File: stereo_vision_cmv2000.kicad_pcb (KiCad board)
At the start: 4 copper layers, 50 x 40 mm, 79 parts, among them P101 CONN_51, P102 CONN_33, U201 AP1084, U202 MCP1826S, U203 RT9017-20GBR, U301 CMV2000, U401 MOUNTHOLE, U402 MOUNTHOLE, U403 MOUNTHOLE, U404 MOUNTHOLE, U405 MOUNTHOLE, U406 MOUNTHOLE, U407 MOUNTHOLE, U408 MOUNTHOLE, U501 24AA025E48

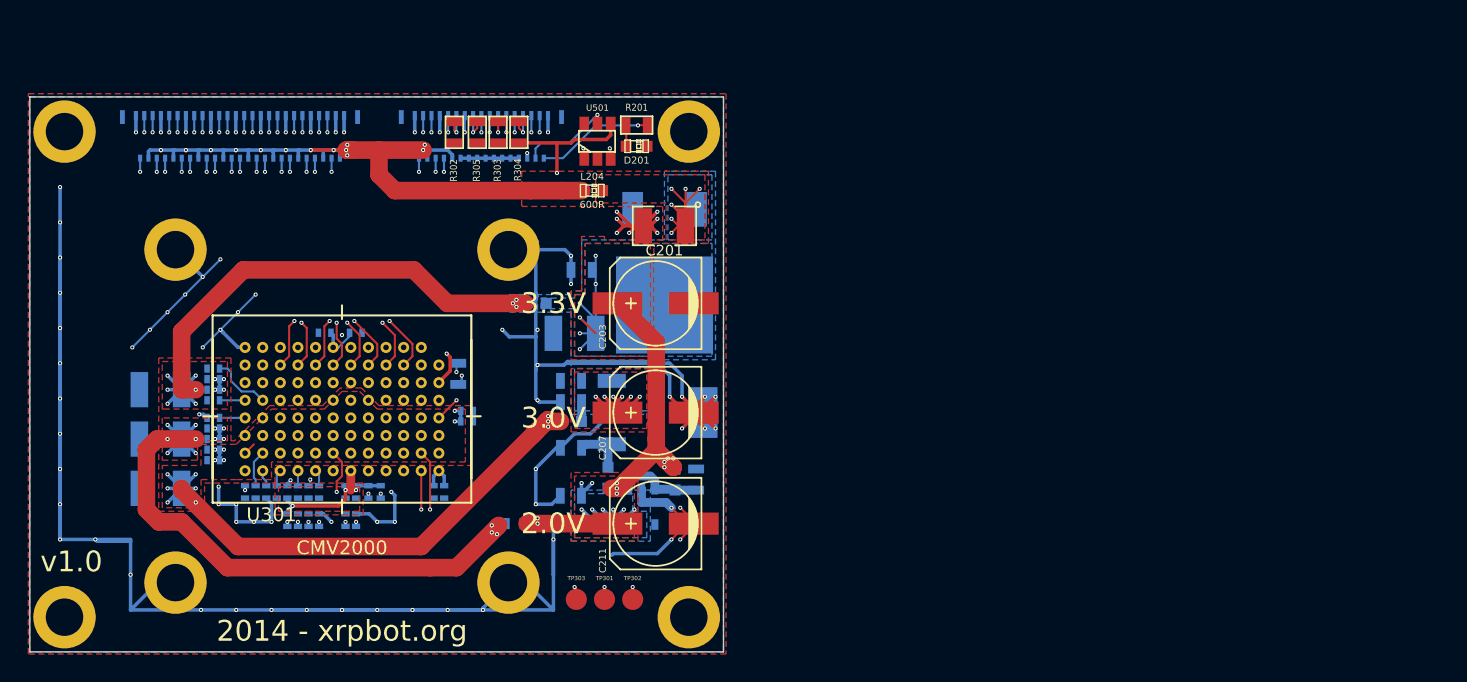
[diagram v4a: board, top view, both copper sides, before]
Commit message: Increase via size
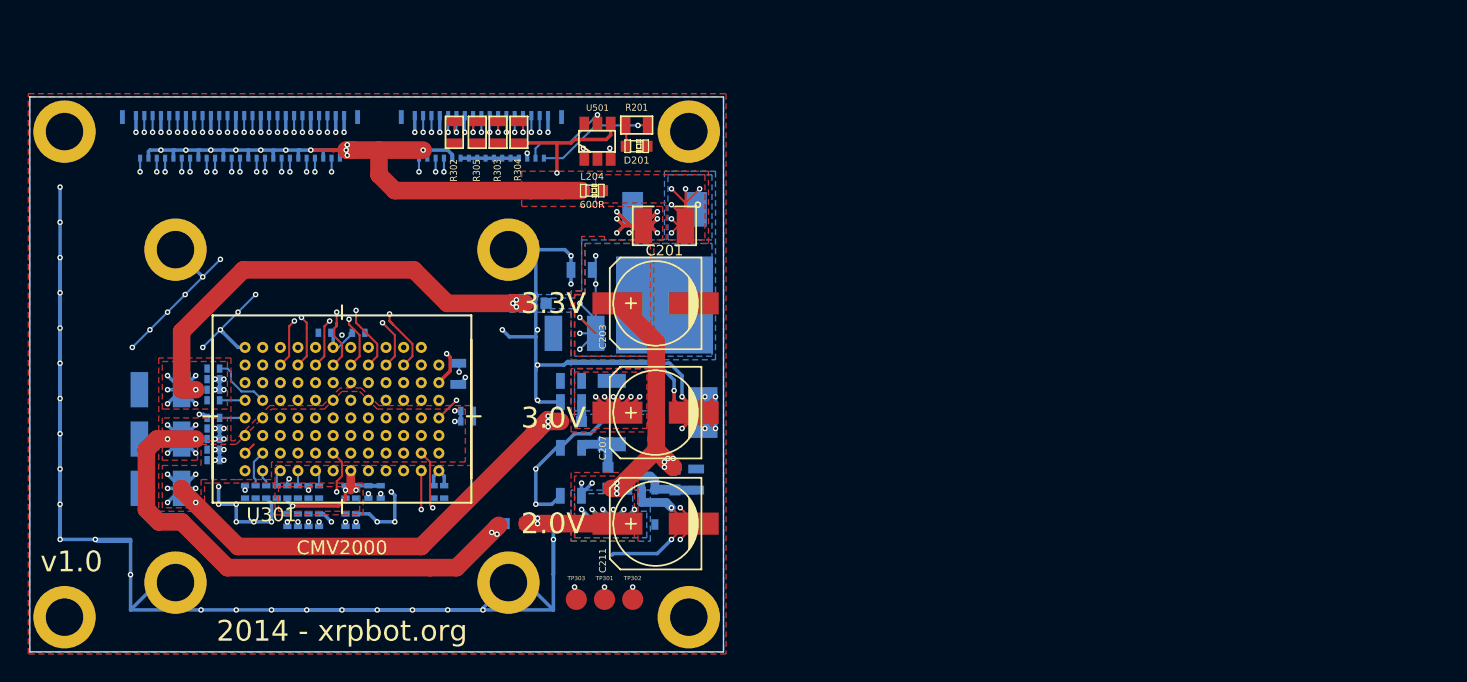
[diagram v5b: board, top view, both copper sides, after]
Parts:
- moved C306 0.20 mm to (132.0, 110.1)
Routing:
- net /Sheet53D8E0E2/SDA: track 8.12 -> 9.09 mm
- net /CMV2000/3.3V: track 107.3 -> 108.2 mm
- net /CMV2000/LVDS_CLK_IN_P: track 24.4 -> 25.2 mm
- net Net-(C340-Pad2): track 4.04 -> 4.81 mm
- net /CMV2000/LVDS_10_N: track 21.8 -> 22.4 mm
- net /CMV2000/SYS_RES_N: track 40.8 -> 40.2 mm
- net GND: track 304.0 -> 304.5 mm
- net /CMV2000/2.0V: track 66.2 -> 65.9 mm, vias 13 -> 12
- net /Power Supply/5V: vias 13 -> 11
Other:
- net class Default: via_dia 0.3 -> 0.4; via_drill 0.25 -> 0.3
- net class Power: via_dia 0.3 -> 0.4; via_drill 0.25 -> 0.3
- net class Power_thick: via_dia 0.3 -> 0.4; via_drill 0.25 -> 0.3
- net class power_thin: via_dia 0.3 -> 0.4; via_drill 0.25 -> 0.3
- rule via_min_size: 0.3 -> 0.4

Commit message: rework connector design and differential routing
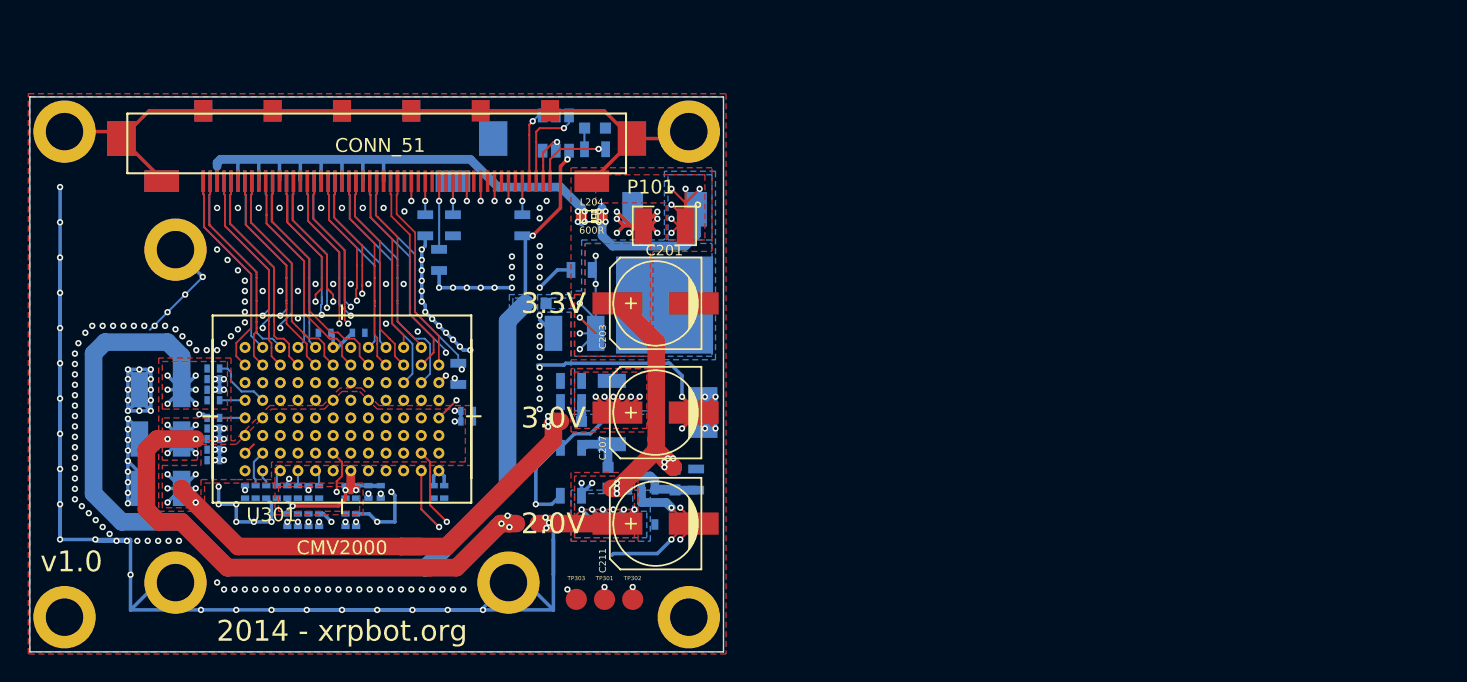
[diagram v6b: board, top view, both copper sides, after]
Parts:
- removed U406: MOUNTHOLE, owncomp:MOUNTING_HOLE
- D201, R201, R302, R303, R304, R305, U501: moved to B.Cu
- P101: footprint owncomp:MOLEX_FPC_0.3mm_51pin -> owncomp:FI-RE51S-HF-R1500; moved to F.Cu
- P102: value CONN_33 -> CONN_31; footprint owncomp:MOLEX_FPC_0.3mm_33pin -> owncomp:FI-RE31S-HF-R1500
- moved P102 13.2 mm to (128.3, 98.6)
- moved P101 10.7 mm to (133.3, 98.6), turned to 180 degrees
- moved R305 9.60 mm to (137.8, 104.8)
- moved R303 7.45 mm to (138.8, 102.3)
- moved R302 7.02 mm to (136.8, 102.3)
- moved R304 6.70 mm to (143.8, 102.3)
- moved R201 3.47 mm to (149.0, 96.8)
- moved D201 3.27 mm to (149.0, 95.3)
- moved U501 3.06 mm to (146.2, 95.7)
- moved L204 1.85 mm to (148.8, 101.7)
- moved L201 1.02 mm to (144.3, 123.8)
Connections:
- P101 pad 1: GND -> /Power Supply/LED_3.3V
- P101 pad 10: /Power Supply/5V -> GND
- P101 pad 11: /CMV2000/LVDS_13_N -> /CMV2000/SPI_OUT
- P101 pad 12: /CMV2000/LVDS_13_P -> GND
- P101 pad 13: GND -> /CMV2000/SPI_IN
- P101 pad 14: /CMV2000/LVDS_14_N -> GND
- P101 pad 15: /CMV2000/LVDS_14_P -> /CMV2000/T_EXP1
- P101 pad 16: /Power Supply/5V -> GND
- P101 pad 17: /CMV2000/LVDS_12_N -> /CMV2000/T_EXP2
- P101 pad 18: /CMV2000/LVDS_12_P -> GND
- P101 pad 19: GND -> /CMV2000/FRAME_REQ
- P101 pad 2: /CMV2000/LVDS_CLK_OUT_N -> /Sheet53D8E0E2/A0
- P101 pad 20: /CMV2000/LVDS_11_N -> GND
- P101 pad 21: /CMV2000/LVDS_11_P -> /CMV2000/CLK_IN
- P101 pad 22: /Power Supply/5V -> GND
- P101 pad 23: /CMV2000/LVDS_10_N -> /CMV2000/LVDS_CTR_N
- P101 pad 24: /CMV2000/LVDS_10_P -> /CMV2000/LVDS_CTR_P
- P101 pad 26: /CMV2000/LVDS_9_N -> /CMV2000/LVDS_2_N
- P101 pad 27: /CMV2000/LVDS_9_P -> /CMV2000/LVDS_2_P
- P101 pad 28: /Power Supply/5V -> GND
- P101 pad 29: /CMV2000/LVDS_7_N -> /CMV2000/LVDS_4_N
- P101 pad 3: /CMV2000/LVDS_CLK_OUT_P -> /Sheet53D8E0E2/SDA
- P101 pad 30: /CMV2000/LVDS_7_P -> /CMV2000/LVDS_4_P
- P101 pad 32: /CMV2000/LVDS_8_N -> /CMV2000/LVDS_3_N
- P101 pad 33: /CMV2000/LVDS_8_P -> /CMV2000/LVDS_3_P
- P101 pad 34: /Power Supply/5V -> GND
- P101 pad 35: /CMV2000/LVDS_5_N -> /CMV2000/LVDS_8_N
- P101 pad 36: /CMV2000/LVDS_5_P -> /CMV2000/LVDS_8_P
- P101 pad 38: /CMV2000/LVDS_6_N -> /CMV2000/LVDS_9_N
- P101 pad 39: /CMV2000/LVDS_6_P -> /CMV2000/LVDS_9_P
- P101 pad 4: /Power Supply/5V -> /Sheet53D8E0E2/SCL
- P101 pad 40: /Power Supply/5V -> GND
- P101 pad 41: /CMV2000/LVDS_4_N -> /CMV2000/LVDS_7_N
- P101 pad 42: /CMV2000/LVDS_4_P -> /CMV2000/LVDS_7_P
- P101 pad 44: /CMV2000/LVDS_3_N -> /CMV2000/LVDS_10_N
- P101 pad 45: /CMV2000/LVDS_3_P -> /CMV2000/LVDS_10_P
- P101 pad 46: /Power Supply/5V -> GND
- P101 pad 47: /CMV2000/LVDS_2_N -> /CMV2000/LVDS_13_N
- P101 pad 48: /CMV2000/LVDS_2_P -> /CMV2000/LVDS_13_P
- P101 pad 5: /CMV2000/LVDS_15_N -> /CMV2000/SYS_RES_N
- P101 pad 50: /Power Supply/5V -> /CMV2000/LVDS_CLK_OUT_N
- P101 pad 51: GND -> /CMV2000/LVDS_CLK_OUT_P
- P101 pad 52: (no net) -> GND
- P101 pad 53: (no net) -> GND
- P101 pad 6: /CMV2000/LVDS_15_P -> GND
- P101 pad 7: GND -> /CMV2000/SPI_CLK
- P101 pad 8: /CMV2000/LVDS_16_N -> GND
- P101 pad 9: /CMV2000/LVDS_16_P -> /CMV2000/SPI_EN
- P102 pad 1: GND -> /CMV2000/LVDS_15_P
- P102 pad 10: /Power Supply/5V -> /CMV2000/LVDS_12_P
- P102 pad 11: /CMV2000/FRAME_REQ -> /CMV2000/LVDS_12_N
- P102 pad 12: GND -> /Power Supply/5V
- P102 pad 13: /CMV2000/CLK_IN -> /CMV2000/LVDS_11_P
- P102 pad 14: GND -> /CMV2000/LVDS_11_N
- P102 pad 15: /CMV2000/T_EXP2 -> /Power Supply/5V
- P102 pad 16: GND -> /CMV2000/LVDS_6_P
- P102 pad 17: /CMV2000/SPI_IN -> /CMV2000/LVDS_6_N
- P102 pad 18: GND -> /Power Supply/5V
- P102 pad 19: /CMV2000/SPI_OUT -> /CMV2000/LVDS_5_P
- P102 pad 2: /CMV2000/LVDS_1_N -> /CMV2000/LVDS_15_N
- P102 pad 20: GND -> /CMV2000/LVDS_5_N
- P102 pad 21: /CMV2000/T_EXP1 -> /Power Supply/5V
- P102 pad 22: GND -> /CMV2000/LVDS_1_P
- P102 pad 23: /CMV2000/SPI_CLK -> /CMV2000/LVDS_1_N
- P102 pad 24: GND -> /Power Supply/5V
- P102 pad 25: /CMV2000/SPI_EN -> /CMV2000/LVDS_CLK_IN_P
- P102 pad 26: GND -> /CMV2000/LVDS_CLK_IN_N
- P102 pad 27: /CMV2000/SYS_RES_N -> /Power Supply/5V
- P102 pad 28: /Sheet53D8E0E2/SCL -> Net-(P102-Pad28)
- P102 pad 29: /Sheet53D8E0E2/SDA -> Net-(P102-Pad29)
- P102 pad 3: /CMV2000/LVDS_1_P -> /Power Supply/5V
- P102 pad 30: /Sheet53D8E0E2/A0 -> Net-(P102-Pad30)
- P102 pad 32: /Power Supply/LED_3.3V -> GND
- P102 pad 4: /Power Supply/5V -> /CMV2000/LVDS_16_P
- P102 pad 5: /CMV2000/LVDS_CTR_N -> /CMV2000/LVDS_16_N
- P102 pad 6: /CMV2000/LVDS_CTR_P -> /Power Supply/5V
- P102 pad 7: GND -> /CMV2000/LVDS_14_P
- P102 pad 8: /CMV2000/LVDS_CLK_IN_N -> /CMV2000/LVDS_14_N
- P102 pad 9: /CMV2000/LVDS_CLK_IN_P -> /Power Supply/5V
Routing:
- net GND: track 304.5 -> 484.7 mm, vias 84 -> 216
- net /CMV2000/3.3V: track 108.2 -> 126.7 mm, vias 19 -> 17
- net Net-(C201-Pad1): track 11.6 -> 28.0 mm, vias 6 -> 10
- net /Power Supply/5V: track 58.6 -> 71.3 mm, vias 11 -> 4
- net Net-(C210-Pad1): track 29.7 -> 39.8 mm, vias 10 -> 11
- net /CMV2000/LVDS_CLK_OUT_P: track 24.1 -> 15.5 mm, vias 1 -> 0
- net /CMV2000/LVDS_15_N: track 23.0 -> 14.5 mm, vias 1 -> 0
- net /CMV2000/LVDS_4_N: track 22.3 -> 14.7 mm, vias 2 -> 0
- net /CMV2000/LVDS_16_P: track 24.3 -> 16.9 mm
- net /CMV2000/LVDS_14_P: track 24.9 -> 17.9 mm
- net /CMV2000/LVDS_12_N: track 20.2 -> 13.3 mm, vias 1 -> 0
- net /CMV2000/LVDS_5_N: track 20.3 -> 13.5 mm, vias 1 -> 0
- net /CMV2000/LVDS_11_P: track 23.3 -> 16.7 mm
- net /CMV2000/LVDS_15_P: track 20.1 -> 13.8 mm, vias 1 -> 0
- net /CMV2000/LVDS_2_N: track 19.5 -> 13.4 mm, vias 1 -> 0
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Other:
- net class Default: clearance 0.15 -> 0.127; trace_width 0.15 -> 0.127; via_dia 0.4 -> 0.4572; via_drill 0.3 -> 0.254
- net class Power: clearance 0.15 -> 0.127; via_dia 0.4 -> 0.4572; via_drill 0.3 -> 0.254
- net class Power_thick: clearance 0.15 -> 0.127; via_dia 0.4 -> 0.4572
- net class power_thin: clearance 0.15 -> 0.127; via_dia 0.4 -> 0.4572
- rule trace_clearance: 0.15 -> 0.127
- rule trace_min: 0.15 -> 0.127
- rule via_min_drill: 0.25 -> 0.254
- rule via_min_size: 0.4 -> 0.4572

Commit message: add values to R302, R303, R305, minor cosmetic fixes, add vias to ground plane
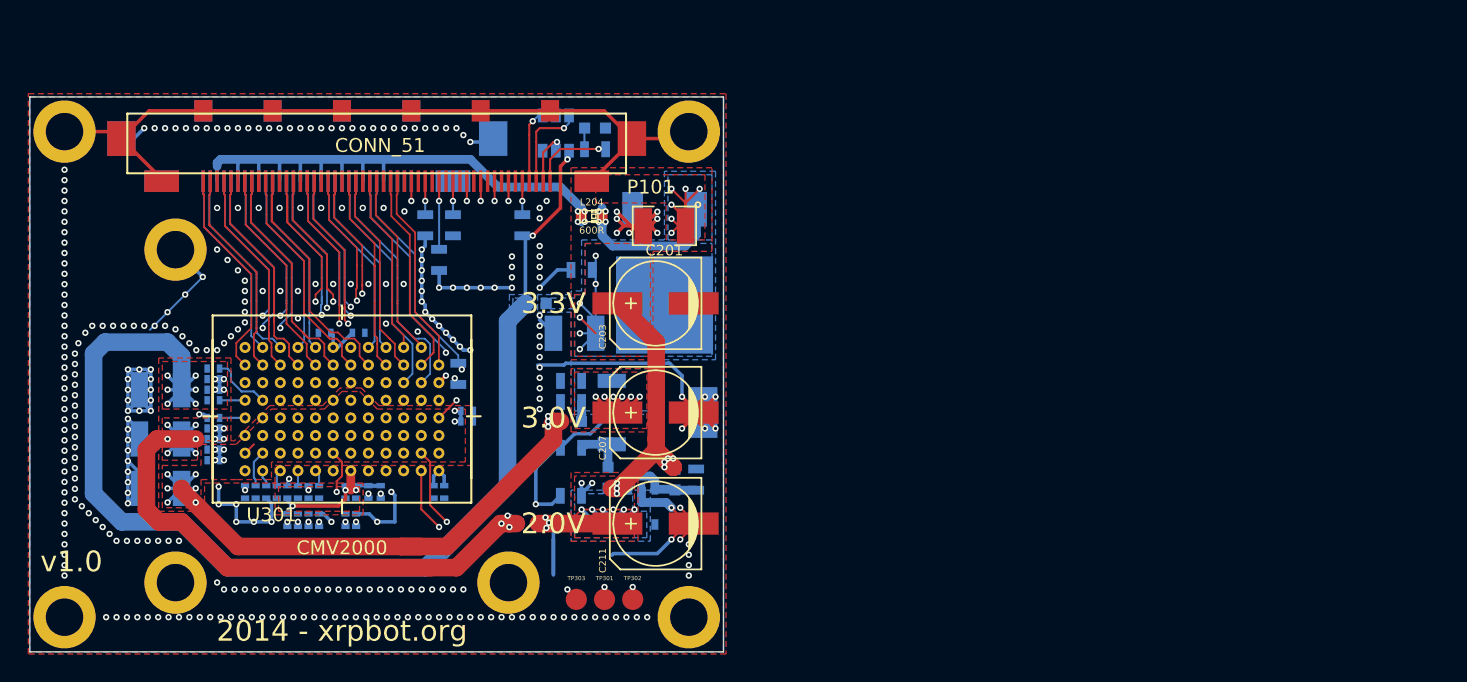
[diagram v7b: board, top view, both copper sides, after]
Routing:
- net GND: track 484.7 -> 469.8 mm, vias 216 -> 324

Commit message: add OSHW logo, cleanup silkscreen
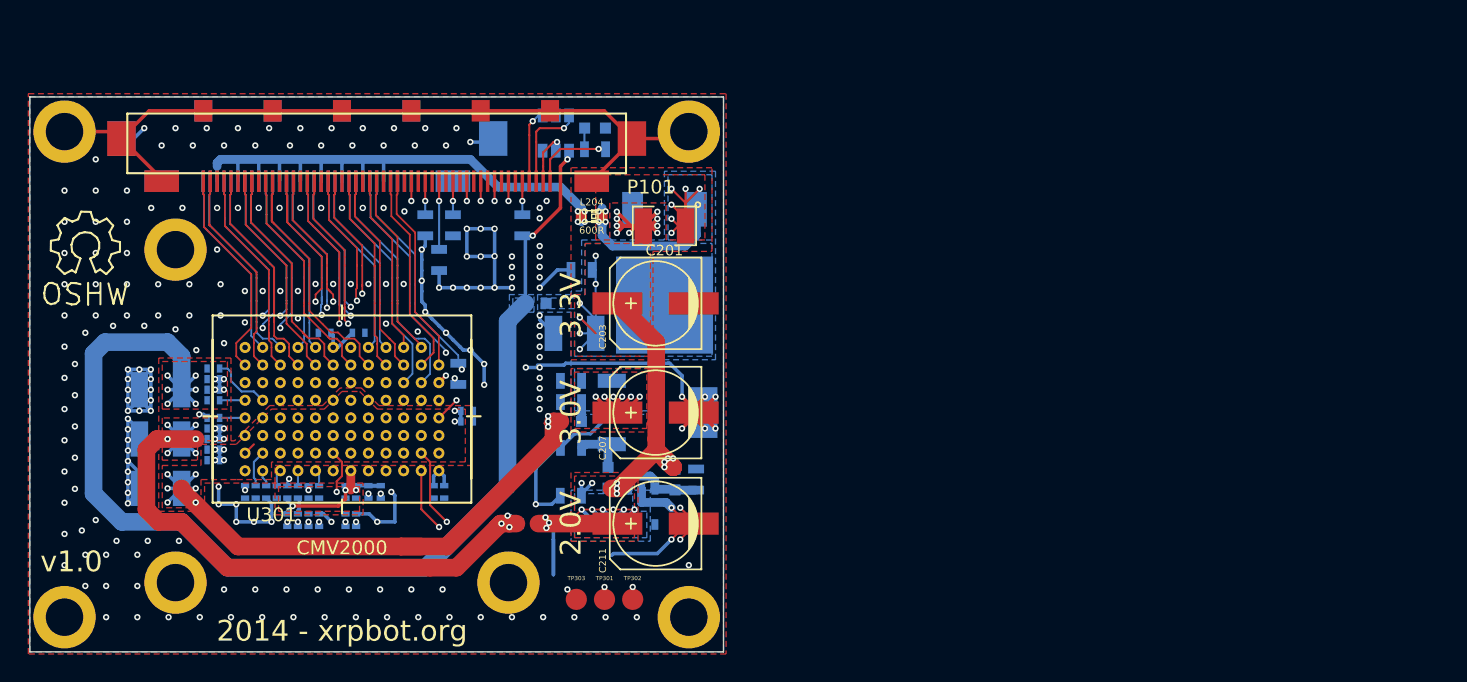
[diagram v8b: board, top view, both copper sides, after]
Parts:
- added SYM: Symbol_OSHW-Logo_SilkScreen_07Jul2012, Symbols:Symbol_OSHW-Logo_SilkScreen, F.Cu at (112.3, 103.8)
- P101: value CONN_51 -> (none)
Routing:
- net GND: track 469.8 -> 570.7 mm, vias 324 -> 221
